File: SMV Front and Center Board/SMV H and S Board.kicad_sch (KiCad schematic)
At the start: 15 parts, among them J1 XT60-M, J2 XT60-M, J3 XT60-M, J4 XT60-M, J5 XT60-M, J6 XT60-M, Q1 PSMN1R8-40YLC_115 - MOSFET, Q3 PSMN1R8-40YLC_115 - MOSFET, U2 TLV76650QWDRBRQ1 (16V->5V), U3 PADS131M04QPWRQ1

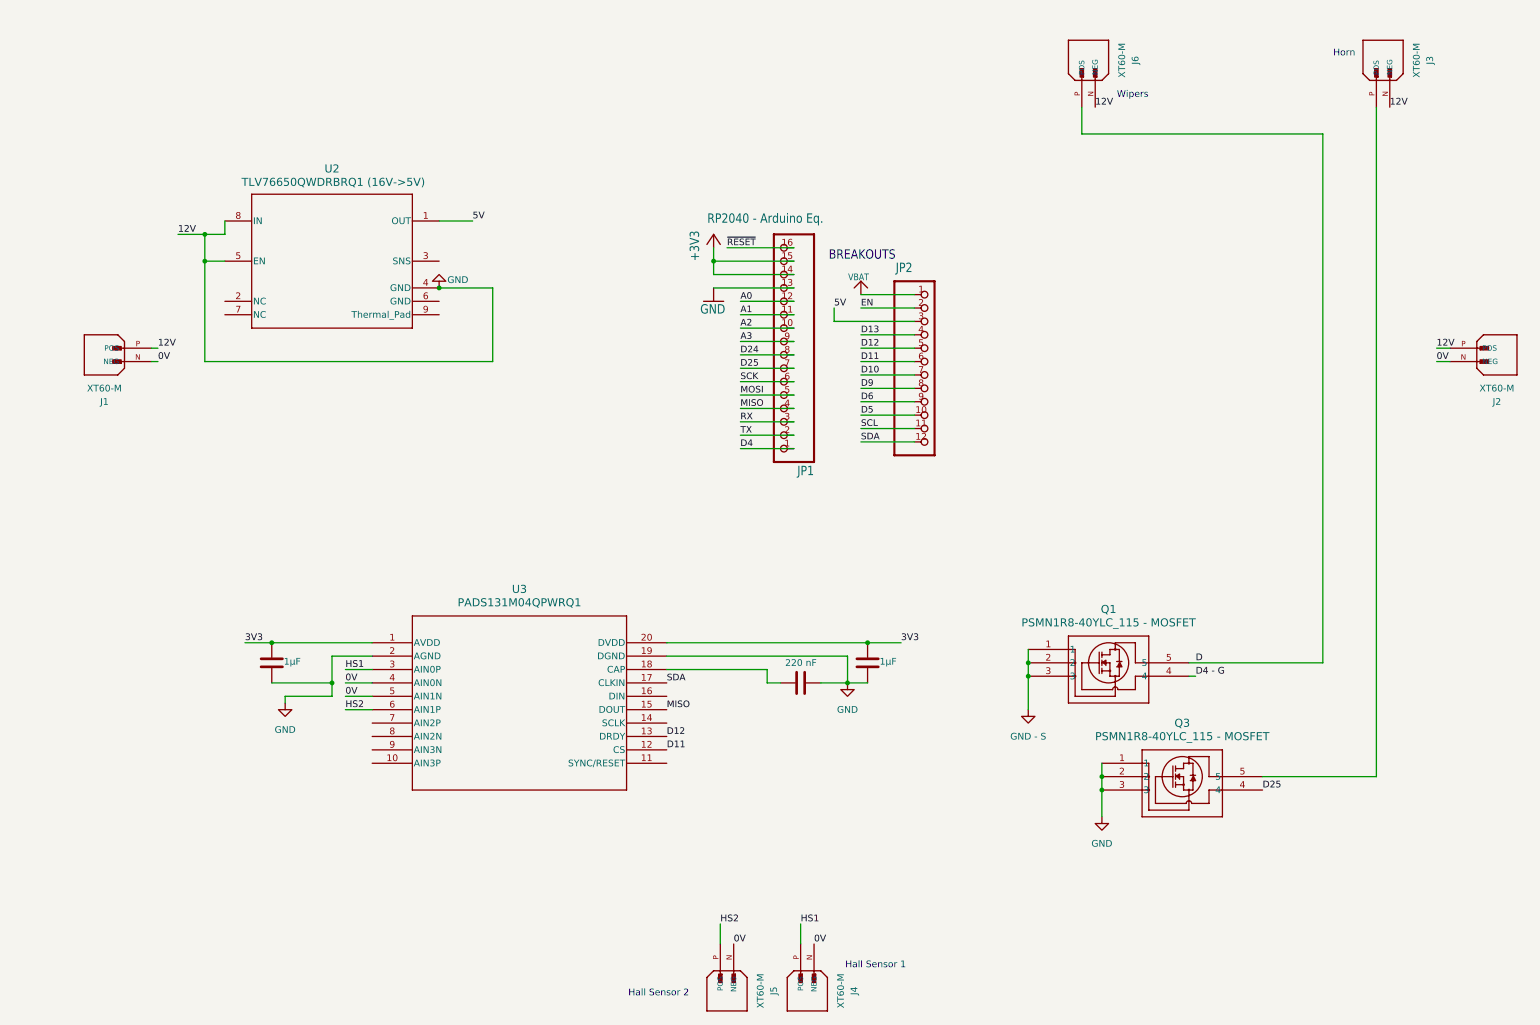
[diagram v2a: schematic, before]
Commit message: Replaced dummy components, added resistors and capactors, replaced Hall Sensor connectors, replaced wiper connector, reorganized components, added visual divisions
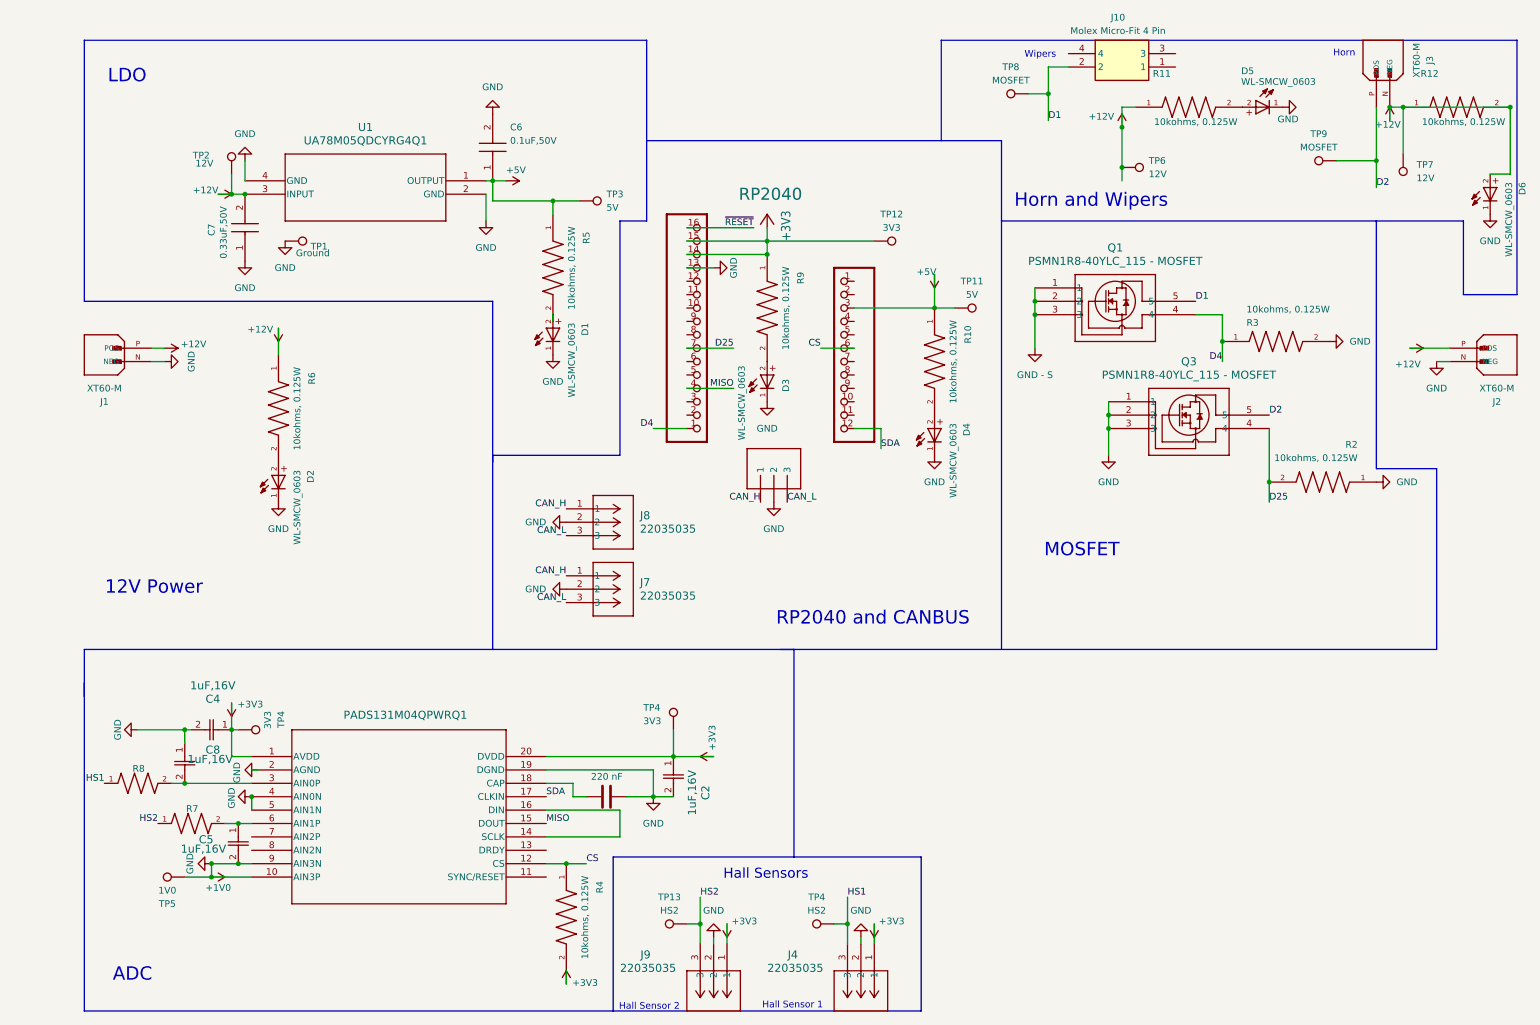
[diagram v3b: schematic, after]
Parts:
- removed C1, C2: 1µF, symbol Device:C
- removed J4, J5, J6: XT60-M, XT60-M:AMASS_XT60-M, symbol XT60-M:XT60-M
- removed JP1: RP2040 - Arduino Eq., Adafruit RP2040 CAN Bus Feather:1X16_ROUND, symbol Adafruit RP2040 CAN Bus Feather-eagle-import:microbuilder_HEADER-1X16ROUND
- removed JP2: HEADER-1X12, Adafruit RP2040 CAN Bus Feather:1X12_ROUND, symbol Adafruit RP2040 CAN Bus Feather-eagle-import:microbuilder_HEADER-1X12
- removed U2: TLV76650QWDRBRQ1 (16V->5V), DRB0008J-IPC_A, symbol TLV76650QWDRBRQ1:TLV76650QWDRBRQ1
- added 3V3 (x2): TP4, TestPoint:TestPoint_Pad_D3.0mm, symbol Connector:TestPoint
- added C2, C4, C5, C8: 1uF,16V, SMV_Passives:Cap0805, symbol SMV_Custom:C0805C105K4RACTU
- added C6: 0.1uF,50V, SMV_Passives:Cap0805, symbol SMV_Custom:C0805C104K5RACTU
- added C7: 0.33uF,50V, SMV_Passives:Cap0805, symbol SMV_Custom:C0805C334K5RACTU
- added D1, D2, D3, D4, D5, D6: WL-SMCW_0603, SMV_Passives:WL-SMCW_0603(diode), symbol SMV_Custom:WL-SMCW_0603
- added J10: Molex Micro-Fit 4 Pin, SMV_Connectors:4_pin0430450401, symbol SMV_Custom:Molex Micro-Fit 4 Pin
- added J4, J7, J8, J9: 22035035, CON_22035035_MOL, symbol SMV_Custom:3-pin Mini Molex Spox
- added R10, R11, R12, R2, R3, R4, R5, R6, R7, R8, R9: 10kohms, 0.125W, SMV_Passives:0805RESC2012X60N, symbol SMV_Custom:CRCW080510K0FKEAC
- added RP2040: ~, SMV_Connectors:RP2040, symbol SMV_Custom:RP2040
- added TP1: Ground, TestPoint:TestPoint_Pad_D3.0mm, symbol Connector:TestPoint
- added TP11, TP3: 5V, TestPoint:TestPoint_Pad_D3.0mm, symbol Connector:TestPoint
- added TP12: 3V3, TestPoint:TestPoint_Pad_D3.0mm, symbol Connector:TestPoint
- added TP13, TP4: HS2, TestPoint:TestPoint_Pad_D3.0mm, symbol Connector:TestPoint
- added TP2, TP6, TP7: 12V, TestPoint:TestPoint_Pad_D3.0mm, symbol Connector:TestPoint
- added TP5: 1V0, TestPoint:TestPoint_Pad_D3.0mm, symbol Connector:TestPoint
- added TP8, TP9: MOSFET, TestPoint:TestPoint_Pad_D3.0mm, symbol Connector:TestPoint
- added U1: UA78M05QDCYRG4Q1, SMV_ICs:DCY4_TEX, symbol SMV_Custom:UA78M05QDCYRG4Q1
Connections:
- net 0V is gone; now on net +1V0: J1.N (NEG), J2.N (NEG), U3.4 (AIN0N), U3.5 (AIN1N)
- net 3V3 is gone; now on net +3V3: U3.1 (AVDD), U3.20 (DVDD)
- net D4 - G is gone; now on net D4: Q1.4
- net +3V3: now also 3V3.1, 3V3.1, C2.1, C4.1, J4.1, J9.1, R4.2, R9.1, RP2040.14, RP2040.15, TP12.1
- net D25: now also R2.2, RP2040.7
- net D4: now also R3.1, RP2040.1
- net HS1: now also J4.3, R8.1, TP4.1; no longer U3.3 (AIN0P)
- net HS2: now also J9.3, R7.1, TP13.1; no longer U3.6 (AIN1P)
- net MISO: now also RP2040.4
- net SDA: now also RP2040.12
- net ~{RESET}: now also RP2040.16
- net D2: now reaches J3.P (POS), Q3.5
- net D2: now also TP9.1
- net +1V0: now reaches U3.10 (AIN3P)
- net +1V0: now also C3.2, Q3.1, Q3.2, Q3.3, U3.19 (DGND), U3.2 (AGND), U3.9 (AIN3N), C2.2, C4.2, C5.2, C6.2, C7.1, C8.1, D1.1, D2.1, D3.1, D4.1, D5.1, D6.1, J4.2, J7.2, J8.2, J9.2, R2.1, R3.2, RP2040.13, RP2040.2, TP1.1, TP5.1, U1.2 (GND), U1.4 (GND)
- net at U3.14 (SCLK): now also U3.16 (DIN)
- net D renamed D1
- net D1: now also J10.2, TP8.1
- net D11 renamed CS
- net CS: now also R4.1, RP2040.6
- net D12: no longer names the net of U3.13 (DRDY)
- removed net GND: C3.2, J1.P (POS), J2.P (POS), J3.N (NEG), Q3.1, Q3.2, Q3.3, U3.19 (DGND), U3.2 (AGND)
- new net: C8.2, R8.2, U3.3 (AIN0P)
- new net: D5.2, R11.2
- new net: C5.1, R7.2, U3.6 (AIN1P)
- new net: D1.2, R5.2
- new net: D2.2, R6.2
- new net: D3.2, R9.2
- new net: D4.2, R10.2
- new net +12V: C7.2, D6.2, J1.P (POS), J2.P (POS), J3.N (NEG), R11.1, R12.1, R12.2, R6.1, TP2.1, TP6.1, TP7.1, U1.3 (INPUT)
- new net +5V: C6.1, R10.1, R5.1, RP2040.3, TP11.1, TP3.1, U1.1 (OUTPUT)
- new net CAN_H: J7.1, J8.1, RP2040.1
- new net CAN_L: J7.3, J8.3, RP2040.3
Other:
- note added: "12V Power"
- note added: "ADC"
- note added: "Hall Sensors"
- note added: "Horn and Wipers"
- note added: "LDO"
- note added: "MOSFET"
- note added: "RP2040 and CANBUS"
- note removed: "BREAKOUTS"
- moved on the sheet: Q1, Q3

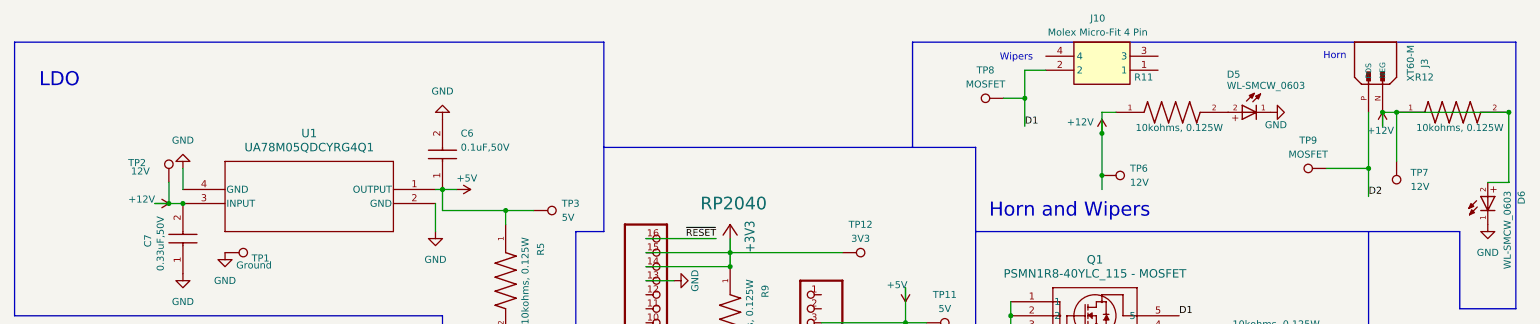
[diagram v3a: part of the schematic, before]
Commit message: Fixed issue with resistor
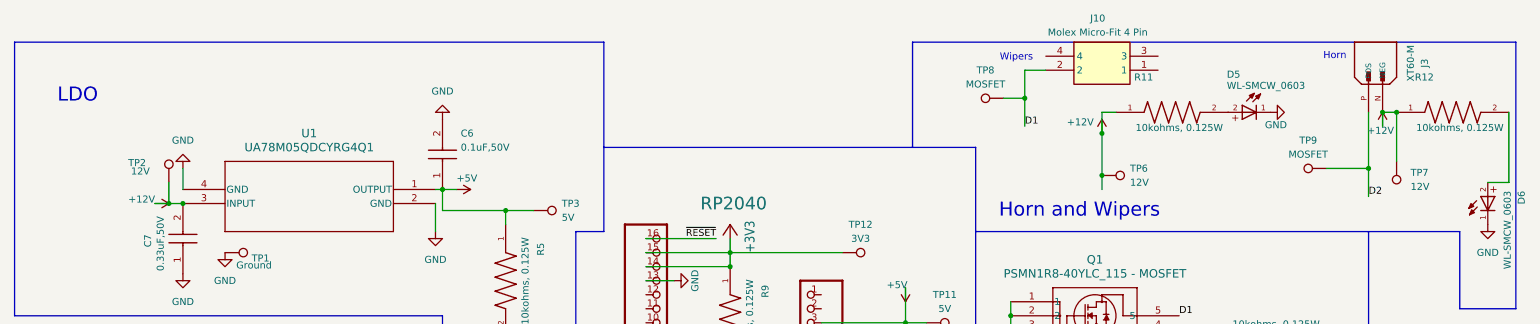
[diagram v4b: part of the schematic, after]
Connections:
- net +12V: no longer D6.2, R12.2
- new net: D6.2, R12.2
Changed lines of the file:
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@@
 	)
 	(junction
-		(at 283.21 25.4)
+		(at 262.89 25.4)
 		(diameter 0)
 		(color 0 0 0 0)
@@
 	)
 	(junction
-		(at 262.89 25.4)
-		(diameter 0)
-		(color 0 0 0 0)
-	)
-	(junction
 		(at 36.83 168.91)
 		(diameter 0)
@@
 	(wire
 		(pts
-			(xy 283.21 38.1) (xy 283.21 25.4)
-		)
-		(stroke
-			(width 0)
-			(type default)
-		)
-	)
-	(wire
-		(pts
 			(xy 154.94 180.34) (xy 157.48 180.34)
 		)
@@
 		(pts
 			(xy 158.75 71.12) (xy 152.4 71.12)
-		)
-		(stroke
-			(width 0)
-			(type default)
-		)
-	)
-	(wire
-		(pts
-			(xy 262.89 25.4) (xy 262.89 34.29)
 		)
 		(stroke
@@
 	(wire
 		(pts
-			(xy 262.89 25.4) (xy 283.21 25.4)
-		)
-		(stroke
-			(width 0)
-			(type default)
-		)
-	)
-	(wire
-		(pts
 			(xy 127 78.74) (xy 135.89 78.74)
 		)
@@
 		(pts
 			(xy 90.17 62.23) (xy 90.17 92.71)
+		)
+		(stroke
+			(width 0)
+			(type default)
+		)
+	)
+	(wire
+		(pts
+			(xy 262.89 25.4) (xy 262.89 34.29)
+		)
+		(stroke
+			(width 0)
+			(type default)
+		)
+	)
+	(wire
+		(pts
+			(xy 283.21 25.4) (xy 283.21 38.1)
 		)
 		(stroke
@@
 	(text "LDO"
 		(exclude_from_sim no)
-		(at 20.828 19.558 0)
+		(at 24.13 22.352 0)
 		(effects
 			(font
@@
 	(text "Horn and Wipers"
 		(exclude_from_sim no)
-		(at 203.708 43.18 0)
+		(at 205.486 43.18 0)
 		(effects
 			(font

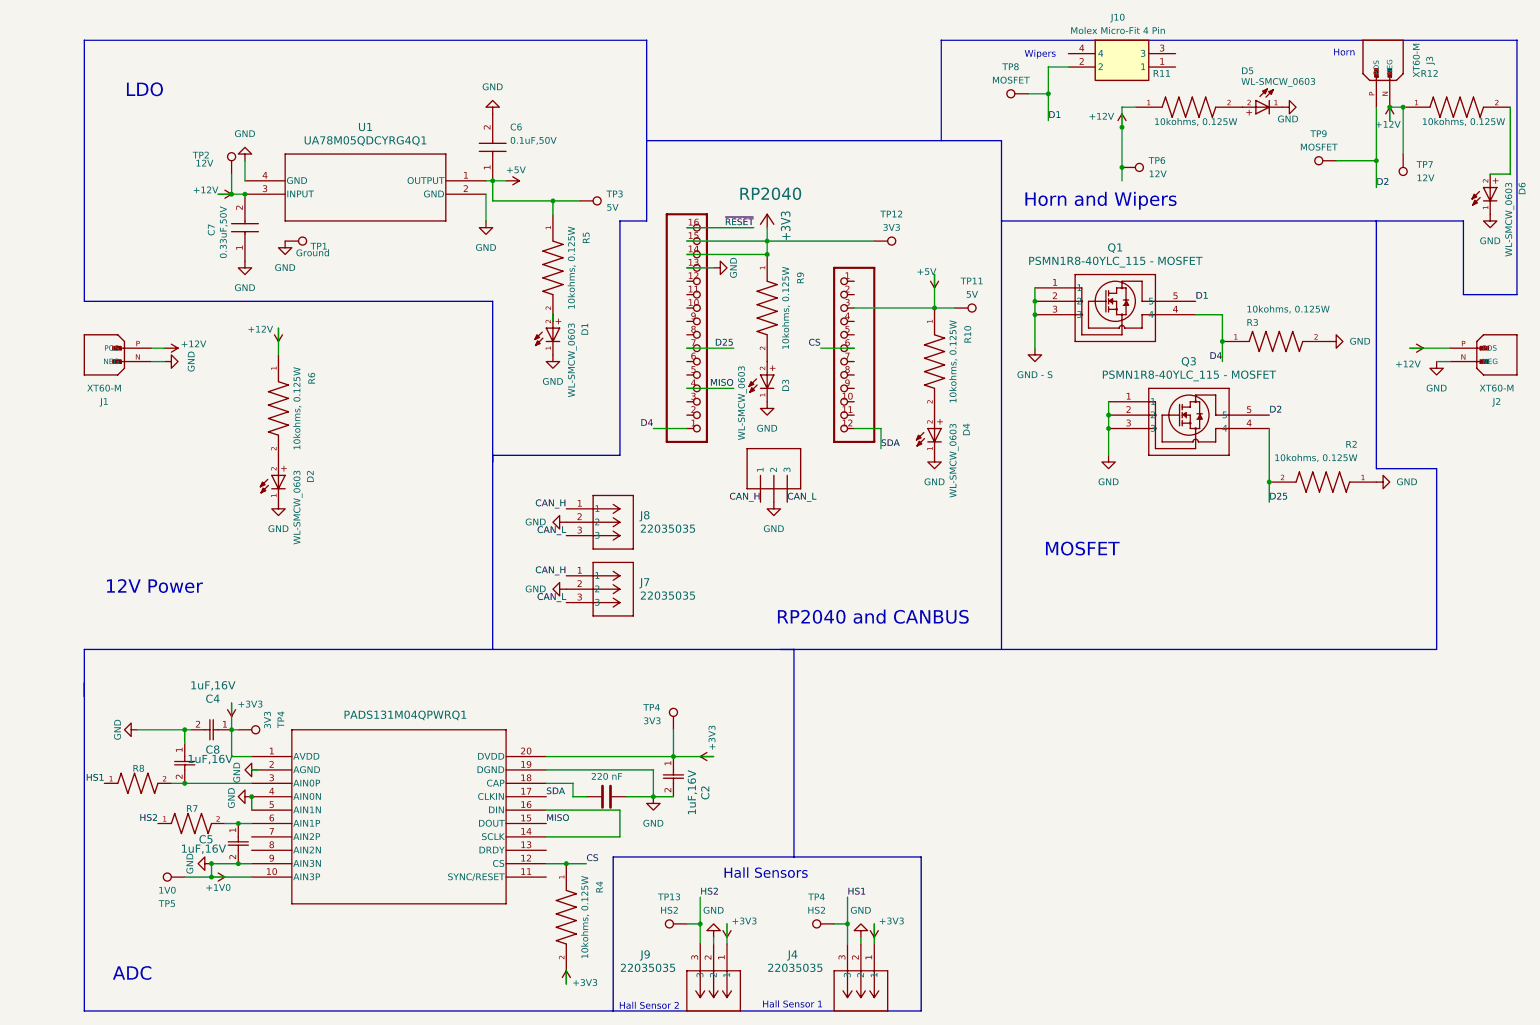
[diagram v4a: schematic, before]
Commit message: Implemented new feedback
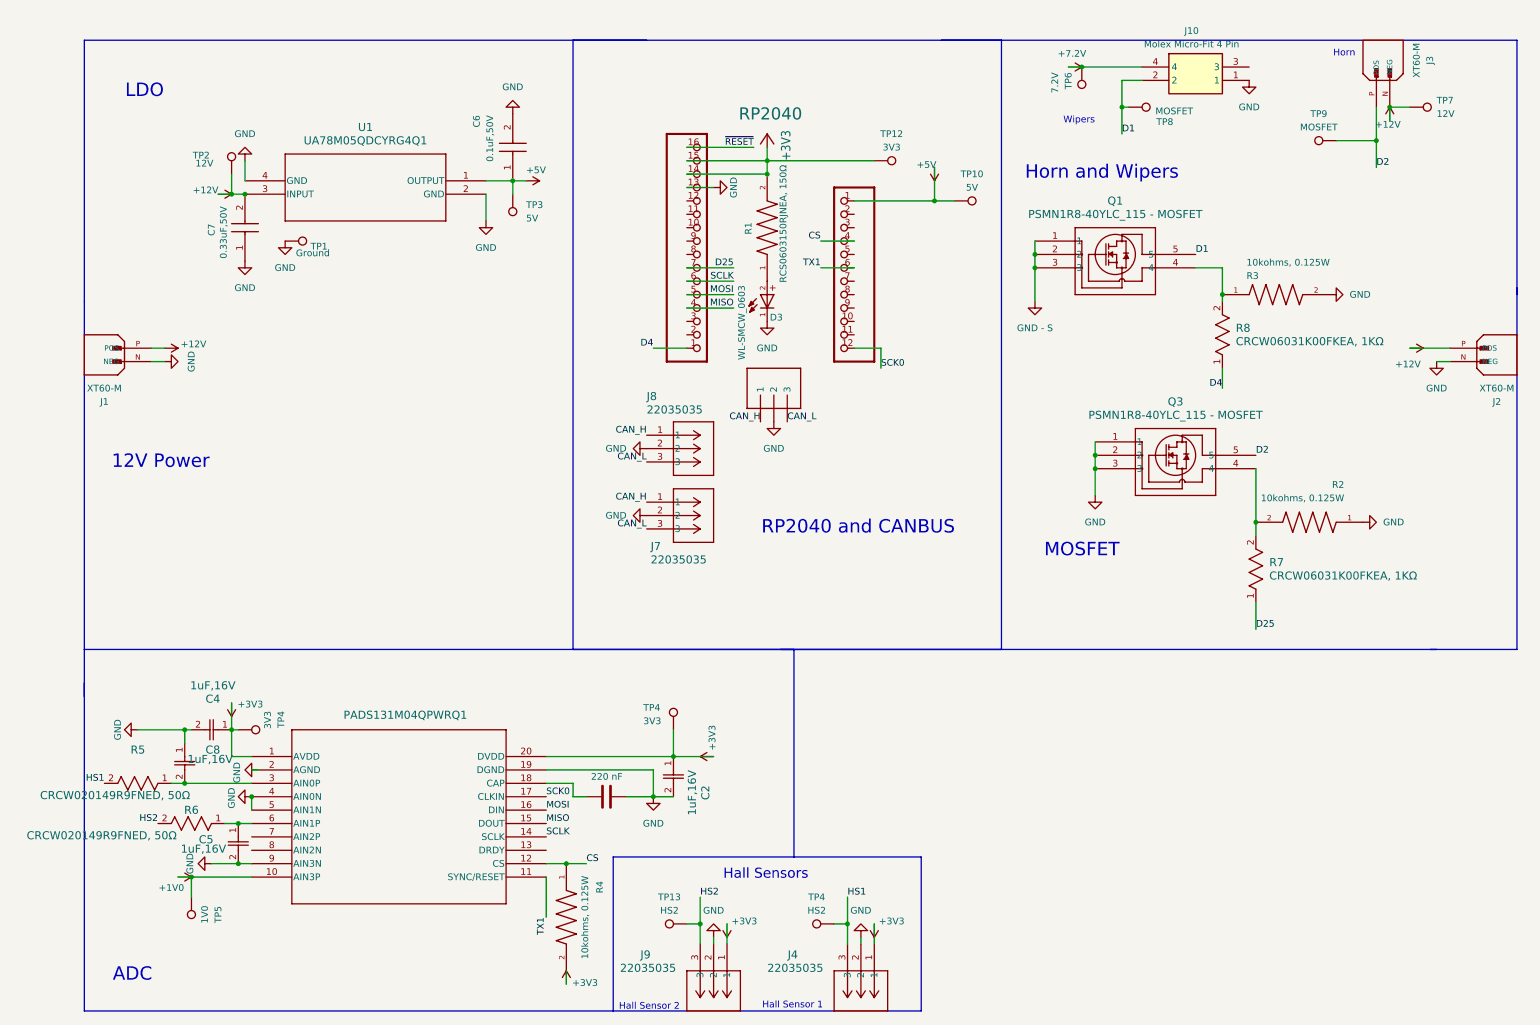
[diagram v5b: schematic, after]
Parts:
- removed D1, D2, D4, D5, D6: WL-SMCW_0603, SMV_Passives:WL-SMCW_0603(diode), symbol SMV_Custom:WL-SMCW_0603
- removed R10, R11, R12, R5, R6, R7, R8, R9: 10kohms, 0.125W, SMV_Passives:0805RESC2012X60N, symbol SMV_Custom:CRCW080510K0FKEAC
- removed TP11: 5V, TestPoint:TestPoint_Pad_D3.0mm, symbol Connector:TestPoint
- added R1: RCS0603150RJNEA, 150Ω, SMV_Passives:0805RESC2012X60N, symbol SMV_Custom:RCS0603150RJNEA
- added R5, R6: CRCW020149R9FNED, 50Ω, SMV_Passives:0805RESC2012X60N, symbol SMV_Custom:CRCW020149R9FNED
- added R7, R8: CRCW06031K00FKEA, 1KΩ, SMV_Passives:0805RESC2012X60N, symbol SMV_Custom:CRCW06031K00FKEA
- added TP10: 5V, TestPoint:TestPoint_Pad_D3.0mm, symbol Connector:TestPoint
- TP6: value 12V -> 7.2V
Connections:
- net SDA is gone; now on net SCK0: RP2040.12, U3.17 (CLKIN)
- net +12V: no longer TP6.1
- net +1V0: no longer C2.2, C3.2, C4.2, C5.2, C6.2, C7.1, C8.1, D3.1, J1.N (NEG), J2.N (NEG), J4.2, J7.2, J8.2, J9.2, Q3.1, Q3.2, Q3.3, R2.1, R3.2, RP2040.13, RP2040.2, TP1.1, U1.2 (GND), U1.4 (GND), U3.19 (DGND), U3.2 (AGND), U3.4 (AIN0N), U3.5 (AIN1N), U3.9 (AIN3N)
- net +3V3: now also R1.2
- net +5V: now also RP2040.1, TP10.1; no longer RP2040.3
- net CS: now also RP2040.4; no longer RP2040.6
- net D25: now also R7.1; no longer Q3.4, R2.2
- net D4: now also R8.1; no longer Q1.4, R3.1
- net HS1: now also R5.2
- net HS2: now also R6.2
- net at C8.2, U3.3 (AIN0P): now also R5.1
- net TX1: now reaches U3.11 (SYNC/RESET)
- net TX1: now also RP2040.6
- net MOSI: now reaches U3.16 (DIN)
- net MOSI: now also RP2040.5; no longer U3.14 (SCLK)
- net at C5.1, U3.6 (AIN1P): now also R6.1
- net SCK0: now reaches RP2040.12
- net GND: now reaches RP2040.2
- net GND: now also C2.2, C3.2, C4.2, C5.2, C6.2, C7.1, C8.1, D3.1, J1.N (NEG), J10.1, J2.N (NEG), J4.2, J7.2, J8.2, J9.2, Q3.1, Q3.2, Q3.3, R2.1, R3.2, RP2040.13, TP1.1, U1.2 (GND), U1.4 (GND), U3.19 (DGND), U3.2 (AGND), U3.4 (AIN0N), U3.5 (AIN1N), U3.9 (AIN3N)
- net at D3.2: now also R1.1
- net +7.2V: now reaches J10.4
- net +7.2V: now also TP6.1
- new net: Q3.4, R2.2, R7.2
- new net: Q1.4, R3.1, R8.2
- new net SCLK: RP2040.6, U3.14 (SCLK)
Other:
- moved on the sheet: C6, D3, J10, J7, J8, Q1, Q3, R2, R3, RP2040, TP12, TP3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
